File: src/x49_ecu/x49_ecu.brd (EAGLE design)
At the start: 134.6 x 101.6 mm, 13 parts, among them J1 1-776163-4, J2 DTP13-4P

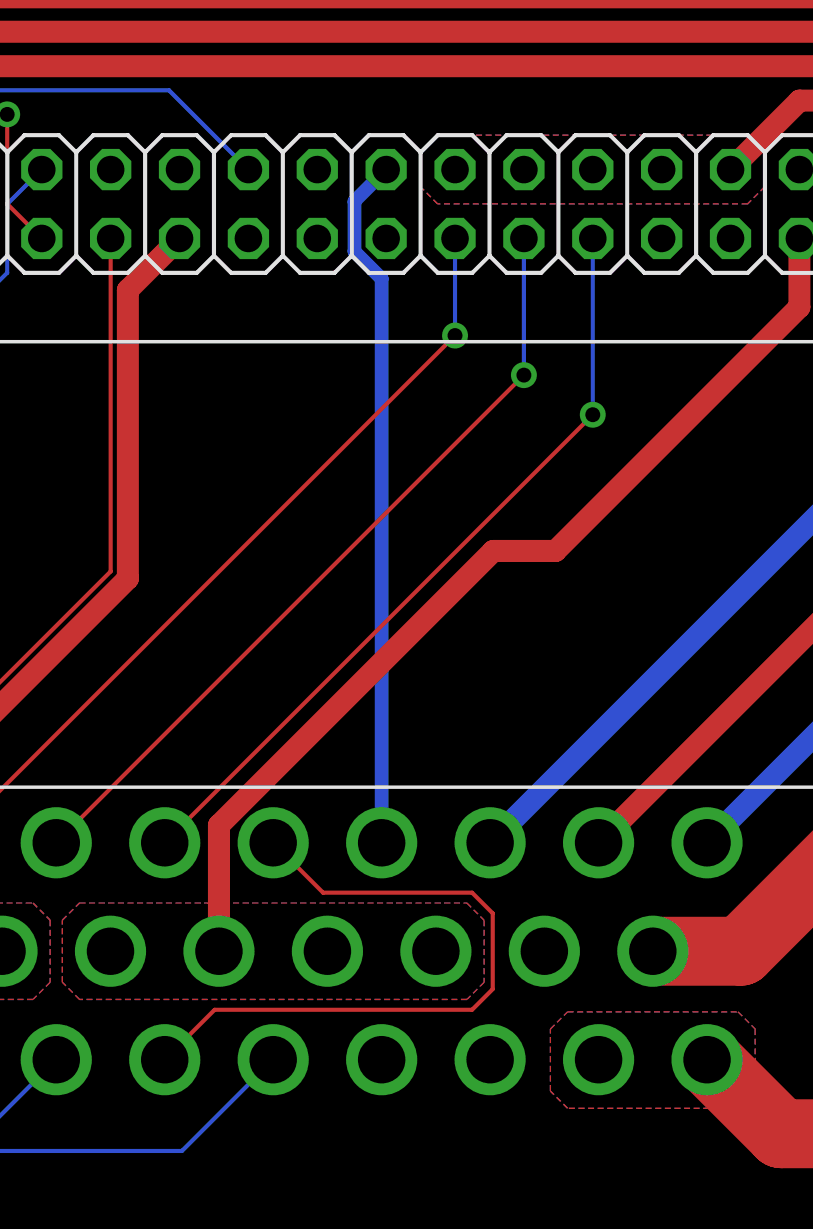
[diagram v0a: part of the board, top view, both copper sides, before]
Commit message: x49_ecu: Connect fan supply to MS FIDLE
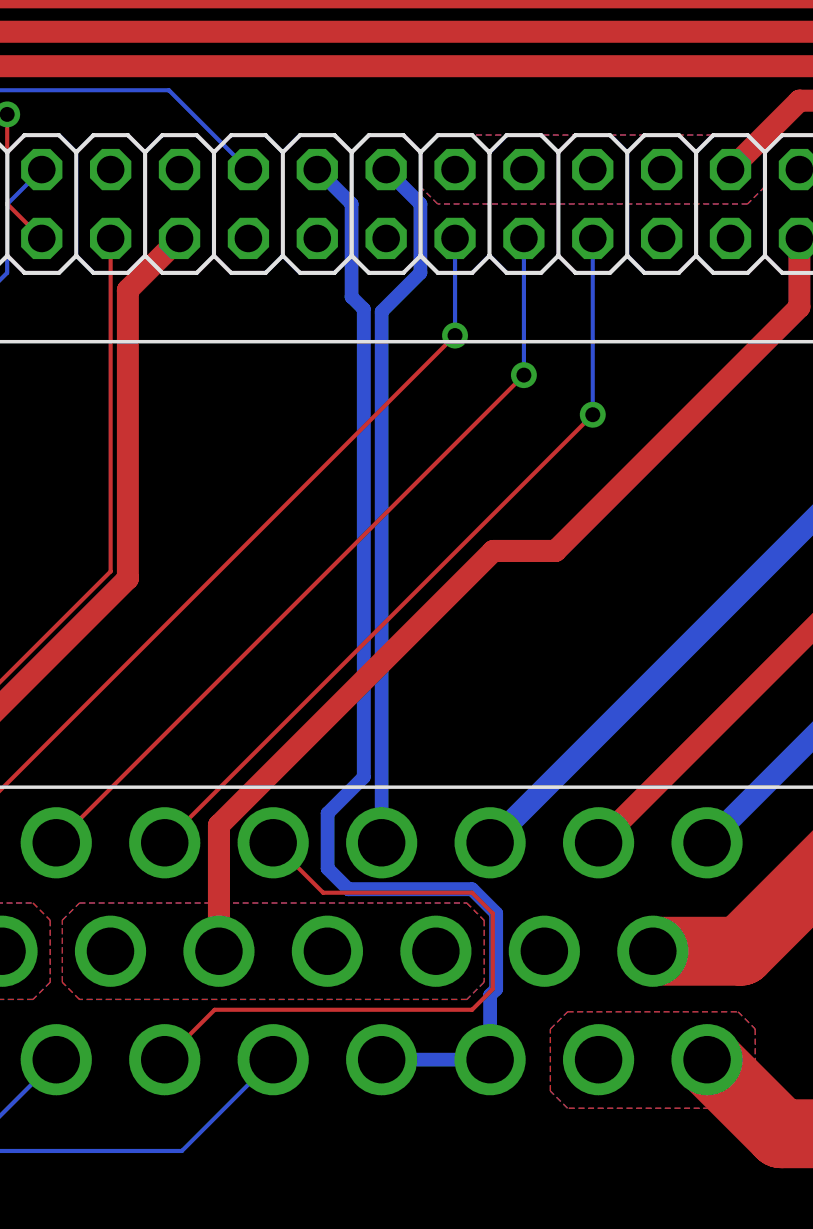
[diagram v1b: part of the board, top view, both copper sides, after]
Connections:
- removed net VDD12V_L_FAN: J1.32
- removed net VDD12V_R_FAN: J1.33
- new net FAN_EN_OUT: J1.32, J1.33, MICROSQUIRT.FIDLE_OUT
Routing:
- net FAN_EN_OUT: track 0.00 -> 43.4 mm
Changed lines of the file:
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@@
 <contactref element="MICROSQUIRT" pad="FUEL_PUMP_OUT"/>
 <contactref element="J1" pad="9"/>
-<wire x1="49.37" y1="15.811" x2="49.37" y2="36.61083125" width="0.508" layer="16"/>
-<wire x1="49.37" y1="36.61083125" x2="48.3676" y2="37.61323125" width="0.508" layer="16"/>
-<wire x1="48.3676" y1="37.61323125" x2="48.3676" y2="39.4688" width="0.508" layer="16"/>
-<wire x1="48.3676" y1="39.4688" x2="49.536" y2="40.6372" width="0.508" layer="16"/>
+<wire x1="49.536" y1="40.6372" x2="49.536" y2="40.634" width="0.508" layer="16"/>
+<wire x1="49.536" y1="40.634" x2="50.8" y2="39.37" width="0.508" layer="16"/>
+<wire x1="50.8" y1="39.37" x2="50.8" y2="36.83" width="0.508" layer="16"/>
+<wire x1="50.8" y1="36.83" x2="49.37" y2="35.4" width="0.508" layer="16"/>
+<wire x1="49.37" y1="15.811" x2="49.37" y2="35.4" width="0.508" layer="16"/>
 </signal>
 <signal name="VDD12V_FUEL_PUMP" class="1">
@@
 <wire x1="39.376" y1="38.0972" x2="39.376" y2="25.817" width="0.1524" layer="1"/>
 </signal>
-<signal name="VDD12V_L_FAN">
-<contactref element="J1" pad="32"/>
-</signal>
-<signal name="VDD12V_R_FAN">
-<contactref element="J1" pad="33"/>
-</signal>
 <signal name="NEUTRAL_IN">
 <contactref element="J1" pad="8"/>
@@
 <wire x1="53.467" y1="10.414" x2="53.467" y2="13.208" width="0.1524" layer="1"/>
 </signal>
+<signal name="FAN_EN_OUT">
+<contactref element="MICROSQUIRT" pad="FIDLE_OUT"/>
+<contactref element="J1" pad="32"/>
+<contactref element="J1" pad="33"/>
+<wire x1="53.594" y1="10.414" x2="53.594" y2="13.208" width="0.508" layer="16"/>
+<wire x1="53.594" y1="13.208" x2="52.705" y2="14.097" width="0.508" layer="16"/>
+<wire x1="48.14255" y1="14.097" x2="47.377" y2="14.86255" width="0.508" layer="16"/>
+<wire x1="52.705" y1="14.097" x2="48.14255" y2="14.097" width="0.508" layer="16"/>
+<wire x1="46.996" y1="40.6372" x2="48.26" y2="39.3732" width="0.508" layer="16"/>
+<wire x1="48.26" y1="35.941" x2="48.26" y2="39.3732" width="0.508" layer="16"/>
+<wire x1="47.377" y1="14.86255" x2="47.377" y2="16.897" width="0.508" layer="16"/>
+<wire x1="47.377" y1="16.897" x2="48.7096" y2="18.2296" width="0.508" layer="16"/>
+<wire x1="48.7096" y1="35.4914" x2="48.26" y2="35.941" width="0.508" layer="16"/>
+<wire x1="48.7096" y1="18.2296" x2="48.7096" y2="35.4914" width="0.508" layer="16"/>
+<wire x1="49.37" y1="7.811" x2="53.37" y2="7.811" width="0.508" layer="16"/>
+<wire x1="53.37" y1="7.811" x2="53.37" y2="10.19" width="0.508" layer="16"/>
+<wire x1="53.37" y1="10.19" x2="53.594" y2="10.414" width="0.508" layer="16"/>
+</signal>
 </signals>

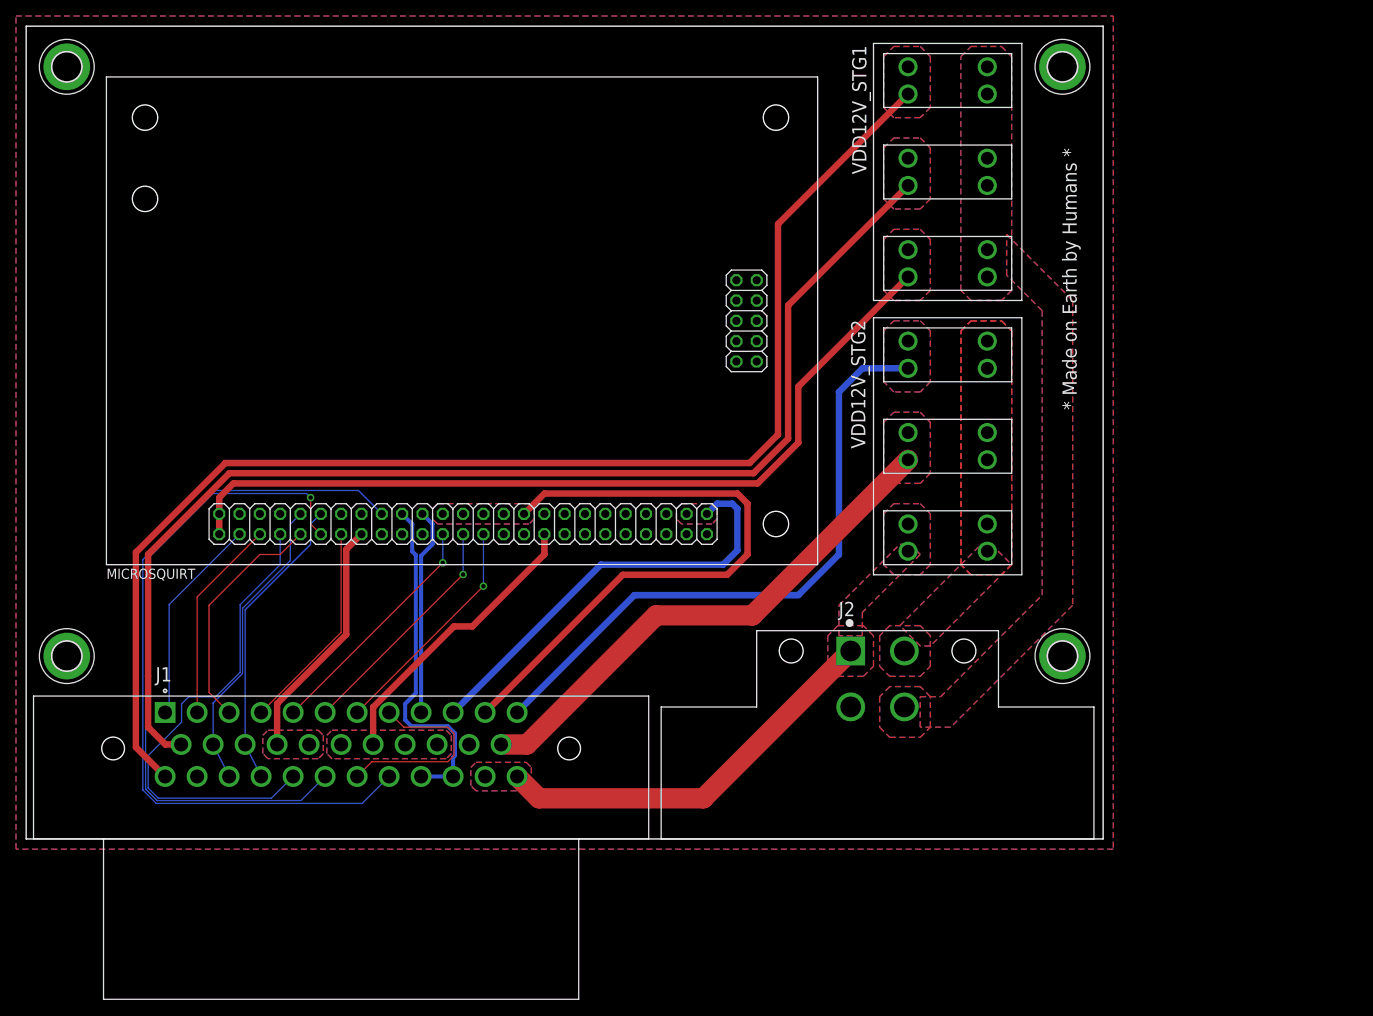
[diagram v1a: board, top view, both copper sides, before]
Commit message: x49_ecu: revision 1a with second DTP connector
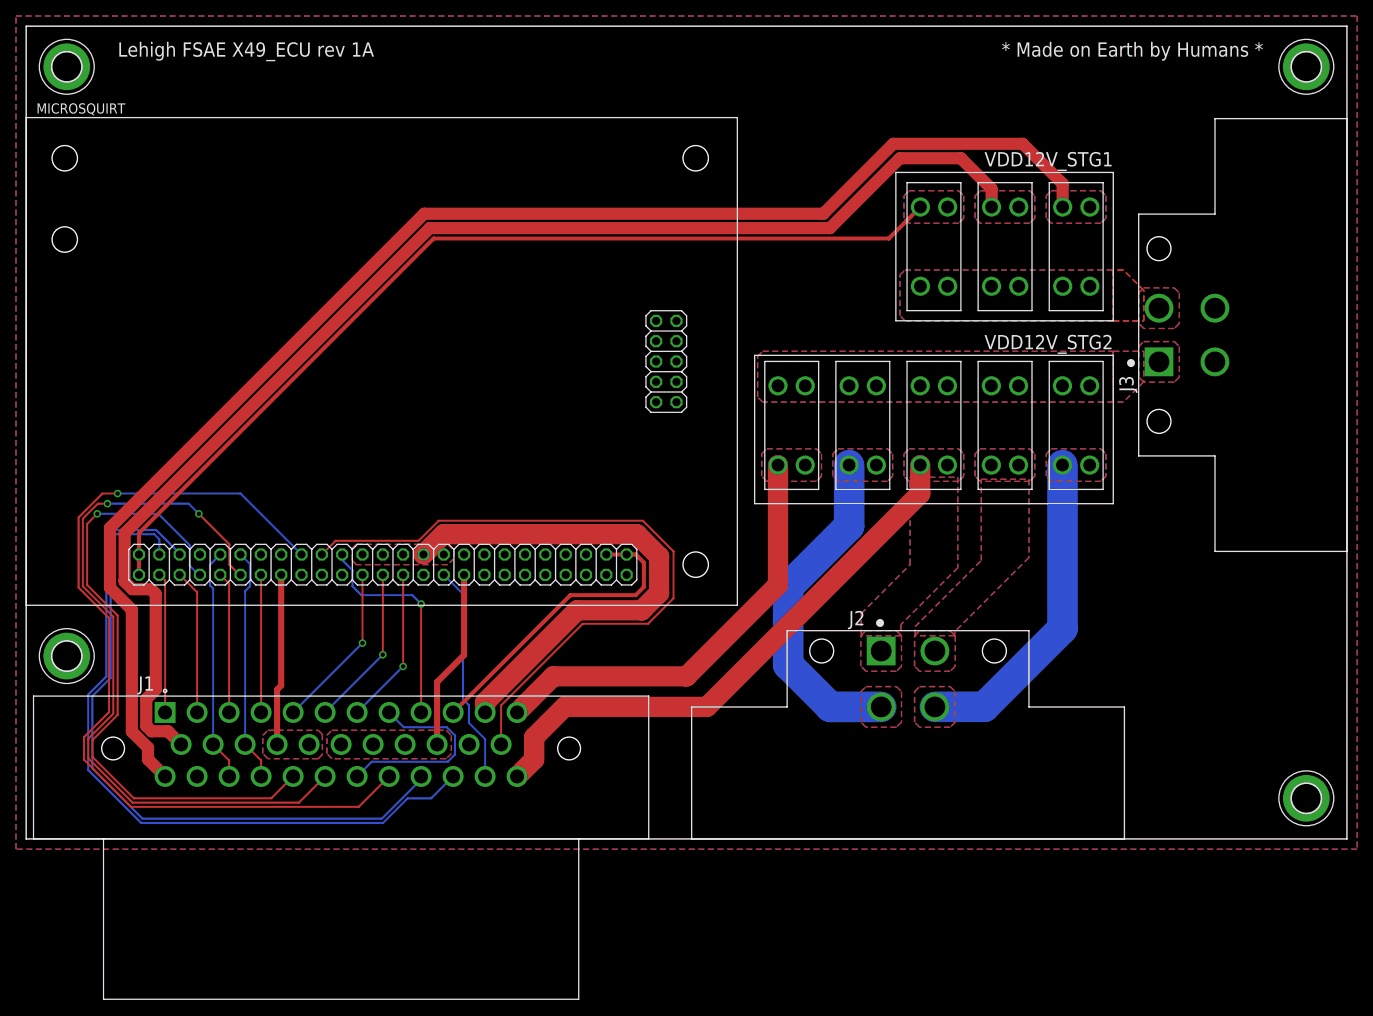
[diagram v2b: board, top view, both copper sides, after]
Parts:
- added J3: DTP13-4P, te_connectivity:TE_DTP13-4P
- added U$8, U$9: 3568, keystone_electronics:3568
- moved H4 35.3 mm to (160.0, 5.08)
- moved H2 30.5 mm to (160.0, 96.5)
- moved U$2 30.3 mm to (133.0, 69.1), turned to 90 degrees
- moved U$5 26.8 mm to (94.0, 56.6), turned to 270 degrees
- moved U$7 19.2 mm to (111.8, 56.6), turned to 270 degrees
- moved U$3 16.5 mm to (124.1, 69.1), turned to 90 degrees
- moved MICROSQUIRT 11.2 mm to (88.9, 29.2)
- moved U$4 6.74 mm to (115.2, 69.1), turned to 90 degrees
- moved U$6 5.86 mm to (120.7, 56.6), turned to 270 degrees
- moved J2 3.81 mm to (110.2, 23.5)
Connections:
- new net SERIAL_GND: J1.34, MICROSQUIRT.SERIAL_GND
- new net SERIAL_RX: J1.32, MICROSQUIRT.SERIAL_RX
- new net SERIAL_TX: J1.33, MICROSQUIRT.SERIAL_TX
- new net VDD12V_FAN_L: J2.4, U$8.R_1, U$8.R_2
- new net VDD12V_FAN_R: J2.3, U$9.R_1, U$9.R_2
- net FAN_EN_OUT: now also J1.23; no longer J1.32, J1.33
- net GND: now also J3.3, J3.4; no longer J2.4
- net VDD12V_FUEL_PUMP: now also J2.2; no longer J1.23
- net VDD12V_IGN_INJ: no longer J1.34
- net VDD12V_STG1: now also J3.2; no longer J2.3
- net VDD12V_STG2: now also J3.1, U$8.L_1, U$8.L_2, U$9.L_1, U$9.L_2; no longer J2.2
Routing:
- net SERIAL_TX: track 0.00 -> 91.6 mm
- net SERIAL_RX: track 0.00 -> 84.2 mm
- net VDD12V_FUEL_PUMP: track 65.6 -> 0.00 mm
- net VDD12V_FAN_L: track 0.00 -> 41.9 mm
- net FAN_EN_OUT: track 43.4 -> 85.1 mm
- net VDD12V_FAN_R: track 0.00 -> 40.5 mm
- net SERIAL_GND: track 0.00 -> 27.3 mm
- net VDD12V_O2: track 78.6 -> 54.2 mm
- net VDD12V_IGN_INJ: track 50.5 -> 70.2 mm
- net ACCEL_LED: track 60.3 -> 79.6 mm, vias 0 -> 1
- net IGN1_OUT: track 53.7 -> 38.5 mm
- net VDD12V_BRAKE_TRANSP: track 150.5 -> 164.5 mm
- net SENSOR_GND: track 36.5 -> 22.6 mm
- net VDD12V_ECU: track 106.2 -> 119.8 mm
- net VDD12V_DASH: track 165.2 -> 177.9 mm
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- added copper zone on layer 1, net VDD12V_FAN_L
- added copper zone on layer 16, net VDD12V_FAN_L
- added copper zone on layer 1, net VDD12V_FAN_R
- added copper zone on layer 16, net VDD12V_FAN_R
- removed copper zone on layer 1, net IGN1_OUT
- removed copper zone on layer 16, net IGN1_OUT
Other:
- board size 134.6 x 101.6 mm -> 165.1 x 101.6 mm
- board text added: "Lehigh FSAE X49_ECU rev 1A"
